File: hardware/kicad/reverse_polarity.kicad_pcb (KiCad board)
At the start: 2 copper layers, 23.6 x 59.8 mm, 17 parts, among them J1 12V_IN, J2 12V_IN, Q1 IRF4905

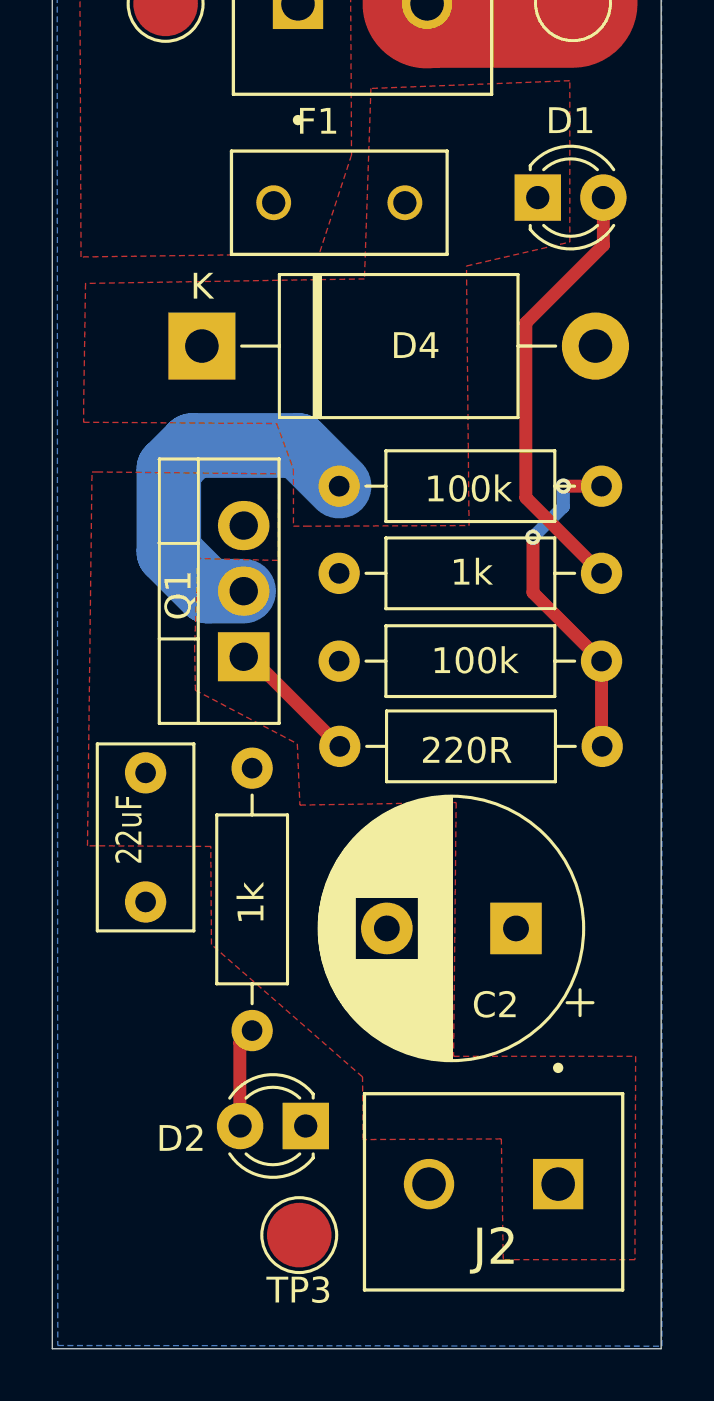
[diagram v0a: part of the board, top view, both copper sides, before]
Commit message: docs: 3d files for design added
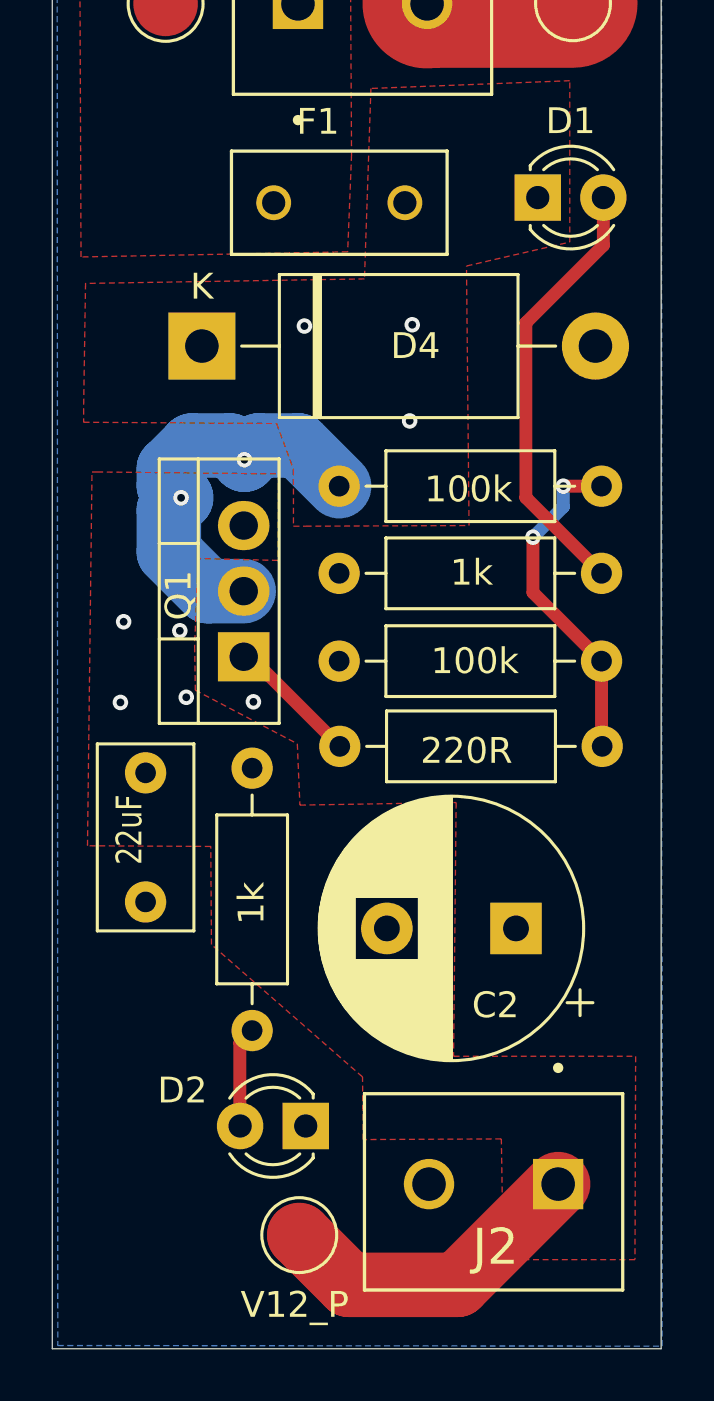
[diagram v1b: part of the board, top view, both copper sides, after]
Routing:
- net /V12_PROT: track 0.00 -> 12.4 mm, vias 0 -> 4
- net /V12_FUSED: track 14.4 -> 15.2 mm, vias 0 -> 5
- net GND: vias 0 -> 1
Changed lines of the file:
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@@
     (property "ki_keywords" "LED diode")
     (attr through_hole)
-    (fp_text reference "D2" (at 4.825 -0.5) (layer "F.SilkS")
+    (fp_text reference "D2" (at 4.775 1.375) (layer "F.SilkS")
         (effects (font (size 1 1) (thickness 0.15)))
     )
@@
     (property "ki_keywords" "test point tp")
     (attr exclude_from_pos_files)
-    (fp_text reference "TP3" (at 0 -2.148) (layer "F.SilkS")
-        (effects (font (size 1 1) (thickness 0.15)))
-    )
-    (fp_text value "V12_P" (at 0 2.25) (layer "F.Fab")
+    (fp_text reference "TP3" (at 0 -2.148) (layer "F.SilkS") hide
+        (effects (font (size 1 1) (thickness 0.15)))
+    )
+    (fp_text value "V12_P" (at 0.175 -2.7) (layer "F.SilkS")
         (effects (font (size 1 1) (thickness 0.15)))
     )
@@
   (segment (start 139.325 56.425) (end 139.3 56.45) (width 5) (layer "F.Cu") (net 1))
   (segment (start 144.95 56.425) (end 139.325 56.425) (width 5) (layer "F.Cu") (net 1))
+  (via (at 132.575 83.475) (size 0.6) (drill 0.3) (layers "F.Cu" "B.Cu") (free) (net 1))
+  (segment (start 134.35 104.125) (end 136.275 106.05) (width 2.5) (layer "F.Cu") (net 2))
+  (segment (start 140.475 106.05) (end 144.375 102.15) (width 2.5) (layer "F.Cu") (net 2))
+  (segment (start 136.275 106.05) (end 140.475 106.05) (width 2.5) (layer "F.Cu") (net 2))
+  (via (at 127.425 83.5) (size 0.6) (drill 0.3) (layers "F.Cu" "B.Cu") (free) (net 2))
+  (via (at 129.725 80.725) (size 0.6) (drill 0.3) (layers "F.Cu" "B.Cu") (free) (net 2))
+  (via (at 127.55 80.375) (size 0.6) (drill 0.3) (layers "F.Cu" "B.Cu") (free) (net 2))
+  (via (at 129.975 83.3) (size 0.6) (drill 0.3) (layers "F.Cu" "B.Cu") (free) (net 2))
   (segment (start 146.125 63.95) (end 146.125 65.8) (width 0.5) (layer "F.Cu") (net 3))
   (segment (start 143.125 75.57) (end 146.055 78.5) (width 0.5) (layer "F.Cu") (net 3))
@@
   (segment (start 144.575 75.925) (end 143.4 77.1) (width 0.5) (layer "B.Cu") (net 7))
   (segment (start 144.575 75.125) (end 144.575 75.925) (width 0.5) (layer "B.Cu") (net 7))
-  (segment (start 129.3 74.45) (end 129.3 77.675) (width 2.5) (layer "B.Cu") (net 8))
+  (via (at 138.625 72.6) (size 0.6) (drill 0.3) (layers "F.Cu" "B.Cu") (free) (net 8))
+  (via (at 138.725 68.875) (size 0.6) (drill 0.3) (layers "F.Cu" "B.Cu") (free) (net 8))
+  (via (at 132.225 74.1) (size 0.6) (drill 0.3) (layers "F.Cu" "B.Cu") (net 8))
+  (via (at 134.55 68.925) (size 0.6) (drill 0.3) (layers "F.Cu" "B.Cu") (free) (net 8))
+  (via (at 129.775 75.575) (size 0.6) (drill 0.3) (layers "F.Cu" "B.Cu") (net 8))
+  (segment (start 129.3 74.45) (end 129.3 75.1) (width 2.5) (layer "B.Cu") (net 8))
+  (segment (start 132.225 74.1) (end 131.675 73.55) (width 2.5) (layer "B.Cu") (net 8))
+  (segment (start 129.3 76.05) (end 129.3 77.675) (width 2.5) (layer "B.Cu") (net 8))
+  (segment (start 131.675 73.55) (end 130.2 73.55) (width 2.5) (layer "B.Cu") (net 8))
+  (segment (start 129.775 75.575) (end 129.3 76.05) (width 2.5) (layer "B.Cu") (net 8))
   (segment (start 130.815 79.19) (end 132.2 79.19) (width 2.5) (layer "B.Cu") (net 8))
+  (segment (start 132.775 73.55) (end 132.225 74.1) (width 2.5) (layer "B.Cu") (net 8))
+  (segment (start 129.3 75.1) (end 129.775 75.575) (width 2.5) (layer "B.Cu") (net 8))
   (segment (start 129.3 77.675) (end 130.815 79.19) (width 2.5) (layer "B.Cu") (net 8))
   (segment (start 135.895 75.125) (end 134.32 73.55) (width 2.5) (layer "B.Cu") (net 8))
   (segment (start 130.2 73.55) (end 129.3 74.45) (width 2.5) (layer "B.Cu") (net 8))
-  (segment (start 134.32 73.55) (end 130.2 73.55) (width 2.5) (layer "B.Cu") (net 8))
+  (segment (start 134.32 73.55) (end 132.775 73.55) (width 2.5) (layer "B.Cu") (net 8))
   (zone (net 8) (net_name "/V12_FUSED") (layer "F.Cu") (name "FUSED") (hatch edge 0.5)
     (priority 2)
@@
         (xy 136.325 53.55)
         (xy 136.375 62.3)
-        (xy 135.125 66.125)
+        (xy 136.225 66.05)
         (xy 125.9 66.25)
       )

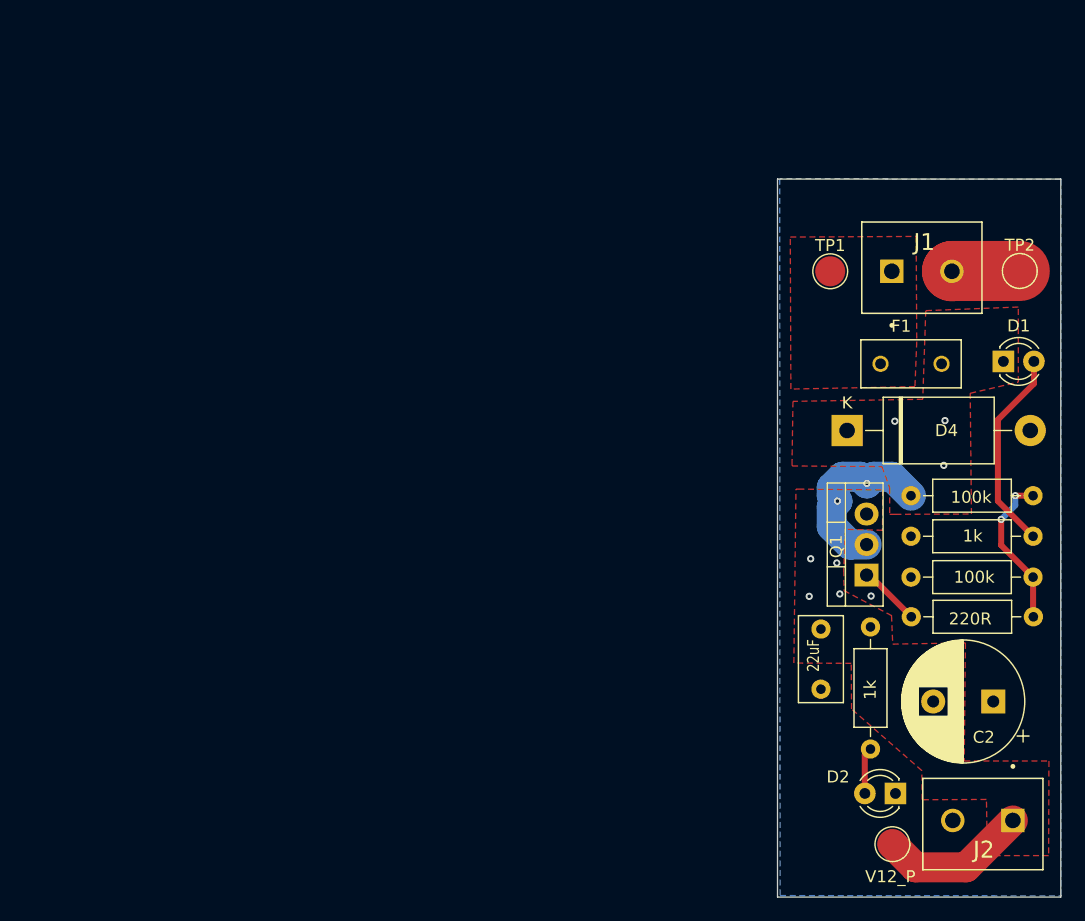
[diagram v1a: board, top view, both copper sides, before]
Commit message: fix: smd packages for reverse polarity & board orientation
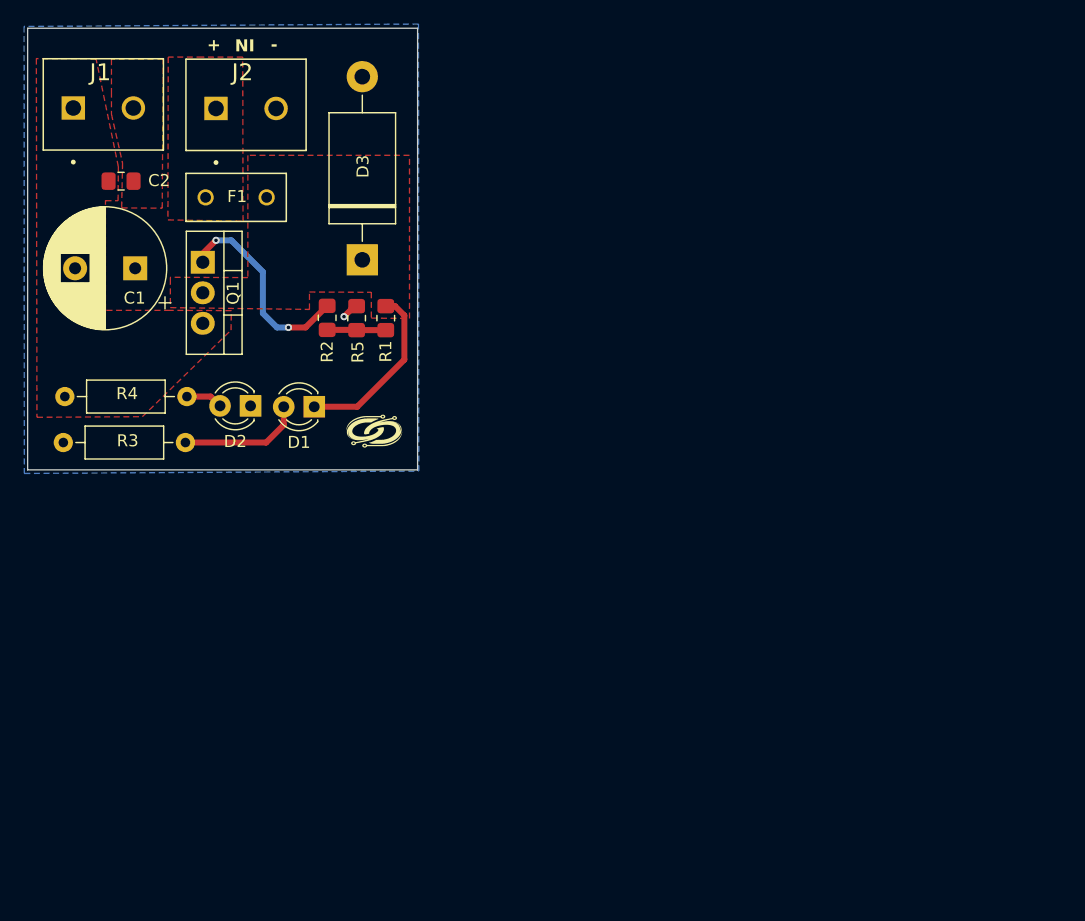
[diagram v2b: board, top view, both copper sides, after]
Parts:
- removed D4: TVS, Diode_THT:D_DO-201AE_P15.24mm_Horizontal
- removed TP1: V12, TestPoint:TestPoint_Pad_D2.5mm
- removed TP2: GND, TestPoint:TestPoint_Pad_D2.5mm
- removed TP3: V12_P, TestPoint:TestPoint_Pad_D2.5mm
- added D3: TVS, Diode_THT:D_DO-201AE_P15.24mm_Horizontal, F.Cu at (90.2, 55.5)
- added G***: LOGO, Logo:logo_pcb, F.Cu at (91.2, 69.9)
- C1: value 22uF -> 470uF; footprint Capacitor_THT:C_Rect_L7.0mm_W3.5mm_P5.00mm -> Capacitor_THT:CP_Radial_D10.0mm_P5.00mm
- C2: value 470uF -> 22uF; footprint Capacitor_THT:CP_Radial_D10.0mm_P5.00mm -> Capacitor_SMD:C_0805_2012Metric_Pad1.18x1.45mm_HandSolder
- R1, R5: value 1k -> 100k; footprint Resistor_THT:R_Axial_DIN0207_L6.3mm_D2.5mm_P10.16mm_Horizontal -> Resistor_SMD:R_0805_2012Metric_Pad1.20x1.40mm_HandSolder
- R2: footprint Resistor_THT:R_Axial_DIN0207_L6.3mm_D2.5mm_P10.16mm_Horizontal -> Resistor_SMD:R_0805_2012Metric_Pad1.20x1.40mm_HandSolder
- R3, R4: value 100k -> 1k
- moved J2 88.9 mm to (78.1, 42.9), turned to 0 degrees
- moved C2 84.5 mm to (70.2, 49.0)
- moved R4 72.0 mm to (65.5, 66.9)
- moved R3 70.7 mm to (65.4, 70.7)
- moved J1 69.5 mm to (66.2, 42.9)
- moved C1 67.0 mm to (71.3, 56.2), turned to 180 degrees
- moved D2 62.6 mm to (80.9, 67.7)
- moved Q1 61.1 mm to (77.0, 55.7), turned to -90 degrees
- moved F1 57.8 mm to (79.7, 50.3)
- moved D1 57.5 mm to (86.2, 67.7), turned to 180 degrees
- moved R2 54.6 mm to (87.3, 60.3), turned to -90 degrees
- moved R5 49.9 mm to (89.8, 60.4)
- moved R1 47.3 mm to (92.2, 60.4), turned to -90 degrees
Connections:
- J1 pad 1: /V12_IN -> /V12_PROT
- J2 pad 1: /V12_PROT -> /V12_IN
- R1 pad 1: GND -> /V12_FUSED
- R1 pad 2: Net-(D1-A) -> Net-(R1-Pad2)
- R2 pad 2: Net-(R2-Pad2) -> Net-(R1-Pad2)
- R3 pad 1: /V12_FUSED -> GND
- R3 pad 2: Net-(R2-Pad2) -> Net-(D1-A)
- R4 pad 1: GND -> /V12_PROT
- R4 pad 2: Net-(R2-Pad2) -> Net-(D2-A)
- R5 pad 1: /V12_PROT -> GND
- R5 pad 2: Net-(D2-A) -> Net-(R1-Pad2)
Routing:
- net Net-(R2-Pad2): track 13.2 -> 0.00 mm, vias 2 -> 0
- net /V12_PROT: track 12.4 -> 0.00 mm, vias 4 -> 0
- net Net-(Q1-G): track 5.16 -> 17.3 mm, vias 0 -> 2
- net Net-(D1-A): track 17.0 -> 10.3 mm
- net Net-(R1-Pad2): track 0.00 -> 4.89 mm
- net GND: track 5.66 -> 1.43 mm
- net Net-(D2-A): track 3.90 -> 3.08 mm
- net /V12_FUSED: track 15.2 -> 14.7 mm, vias 5 -> 0
- added copper zone on F.Cu, net GND
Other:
- board size 23.6 x 59.8 mm -> 32.5 x 36.7 mm
- board text added: "+"
- board text added: "-"
- board text added: "IN"
